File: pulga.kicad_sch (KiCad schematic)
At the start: 32 parts, among them J1 Conn_01x04_Pin, J2 Conn_01x04_Pin, SW1 SW_Push, SW2 SW_Push, U2 ESP32-C3-WROOM-02, U3 TCAN332G, U4 AMS1117-3.3

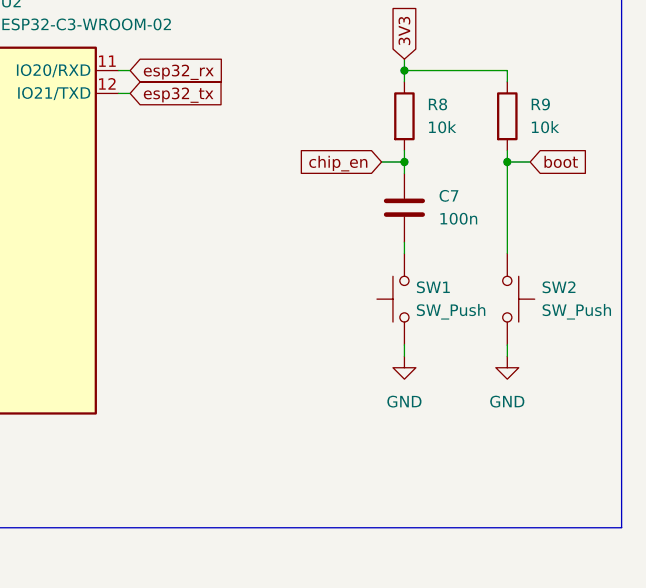
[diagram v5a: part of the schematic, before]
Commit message: corrigindo a posição de C7 para ficar em paralelo em relação a SW1
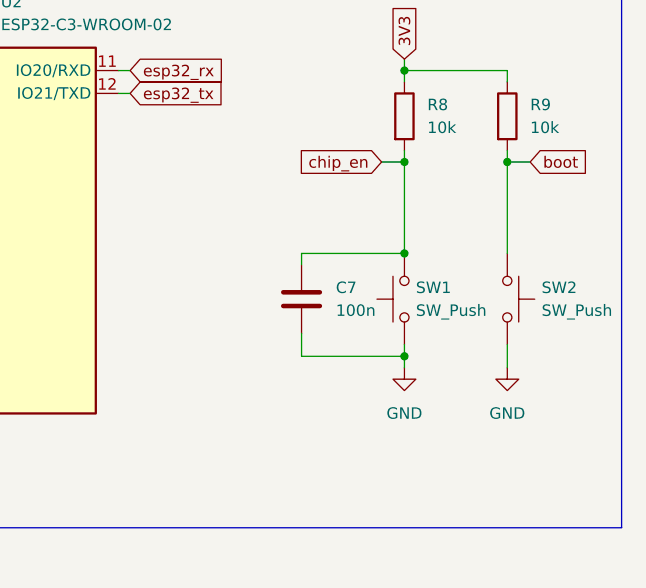
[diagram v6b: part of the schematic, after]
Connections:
- net GND: now also C7.2
- net chip_en: now also SW1.2
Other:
- moved on the sheet: C7
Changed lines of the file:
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@@
 	)
 	(junction
-		(at 256.54 55.88)
-		(diameter 0)
-		(color 0 0 0 0)
-	)
-	(junction
 		(at 46.99 55.88)
 		(diameter 0)
@@
 	)
 	(junction
+		(at 256.54 66.04)
+		(diameter 0)
+		(color 0 0 0 0)
+	)
+	(junction
 		(at 38.1 55.88)
 		(diameter 0)
@@
 	)
 	(junction
+		(at 256.54 77.47)
+		(diameter 0)
+		(color 0 0 0 0)
+	)
+	(junction
 		(at 38.1 33.02)
 		(diameter 0)
@@
 		(color 0 0 0 0)
 	)
+	(junction
+		(at 256.54 55.88)
+		(diameter 0)
+		(color 0 0 0 0)
+	)
 	(wire
 		(pts
@@
 	(wire
 		(pts
-			(xy 267.97 76.2) (xy 267.97 77.47)
+			(xy 256.54 54.61) (xy 256.54 55.88)
+		)
+		(stroke
+			(width 0)
+			(type default)
+		)
+	)
+	(wire
+		(pts
+			(xy 267.97 76.2) (xy 267.97 78.74)
 		)
 		(stroke
@@
 	(wire
 		(pts
+			(xy 245.11 74.93) (xy 245.11 77.47)
+		)
+		(stroke
+			(width 0)
+			(type default)
+		)
+	)
+	(wire
+		(pts
 			(xy 113.03 146.05) (xy 113.03 143.51)
 		)
@@
 	(wire
 		(pts
+			(xy 256.54 55.88) (xy 256.54 66.04)
+		)
+		(stroke
+			(width 0)
+			(type default)
+		)
+	)
+	(wire
+		(pts
 			(xy 237.49 120.65) (xy 240.03 120.65)
 		)
@@
 	(wire
 		(pts
+			(xy 245.11 77.47) (xy 256.54 77.47)
+		)
+		(stroke
+			(width 0)
+			(type default)
+		)
+	)
+	(wire
+		(pts
 			(xy 209.55 86.36) (xy 209.55 87.63)
 		)
@@
 	(wire
 		(pts
-			(xy 256.54 64.77) (xy 256.54 66.04)
-		)
-		(stroke
-			(width 0)
-			(type default)
-		)
-	)
-	(wire
-		(pts
 			(xy 54.61 146.05) (xy 55.88 146.05)
 		)
@@
 	(wire
 		(pts
+			(xy 245.11 66.04) (xy 256.54 66.04)
+		)
+		(stroke
+			(width 0)
+			(type default)
+		)
+	)
+	(wire
+		(pts
 			(xy 44.45 146.05) (xy 46.99 146.05)
 		)
@@
 	(wire
 		(pts
-			(xy 256.54 55.88) (xy 256.54 57.15)
-		)
-		(stroke
-			(width 0)
-			(type default)
-		)
-	)
-	(wire
-		(pts
 			(xy 256.54 76.2) (xy 256.54 77.47)
 		)
@@
 	(wire
 		(pts
-			(xy 256.54 54.61) (xy 256.54 55.88)
+			(xy 36.83 30.48) (xy 38.1 30.48)
 		)
 		(stroke
@@
 	(wire
 		(pts
-			(xy 36.83 30.48) (xy 38.1 30.48)
+			(xy 256.54 78.74) (xy 256.54 77.47)
 		)
 		(stroke
@@
 	(wire
 		(pts
+			(xy 245.11 67.31) (xy 245.11 66.04)
+		)
+		(stroke
+			(width 0)
+			(type default)
+		)
+	)
+	(wire
+		(pts
 			(xy 78.74 161.29) (xy 78.74 162.56)
 		)
@@
 	(symbol
 		(lib_id "Device:C")
-		(at 256.54 60.96 0)
+		(at 245.11 71.12 0)
 		(unit 1)
 		(exclude_from_sim no)
@@
 		(fields_autoplaced yes)
 		(property "Reference" "C7"
-			(at 260.35 59.6899 0)
+			(at 248.92 69.8499 0)
 			(effects
 				(font
@@
 		)
 		(property "Value" "100n"
-			(at 260.35 62.2299 0)
+			(at 248.92 72.3899 0)
 			(effects
 				(font
@@
 		)
 		(property "Footprint" "Capacitor_SMD:C_0201_0603Metric"
-			(at 257.5052 64.77 0)
+			(at 246.0752 74.93 0)
 			(effects
 				(font
@@
 		)
 		(property "Datasheet" "~"
-			(at 256.54 60.96 0)
+			(at 245.11 71.12 0)
 			(effects
 				(font
@@
 		)
 		(property "Description" "Unpolarized capacitor"
-			(at 256.54 60.96 0)
+			(at 245.11 71.12 0)
 			(effects
 				(font
@@
 	(symbol
 		(lib_id "power:GND")
-		(at 256.54 77.47 0)
+		(at 256.54 78.74 0)
 		(unit 1)
 		(exclude_from_sim no)
@@
 		(fields_autoplaced yes)
 		(property "Reference" "#PWR07"
-			(at 256.54 83.82 0)
+			(at 256.54 85.09 0)
 			(effects
 				(font
@@
 		)
 		(property "Value" "GND"
-			(at 256.54 82.55 0)
+			(at 256.54 83.82 0)
 			(effects
 				(font
@@
 		)
 		(property "Footprint" ""
-			(at 256.54 77.47 0)
+			(at 256.54 78.74 0)
 			(effects
 				(font
@@
 		)
 		(property "Datasheet" ""
-			(at 256.54 77.47 0)
+			(at 256.54 78.74 0)
 			(effects
 				(font
@@
 		)
 		(property "Description" "Power symbol creates a global label with name \"GND\" , ground"
-			(at 256.54 77.47 0)
+			(at 256.54 78.74 0)
 			(effects
 				(font
@@
 	(symbol
 		(lib_id "power:GND")
-		(at 267.97 77.47 0)
+		(at 267.97 78.74 0)
 		(unit 1)
 		(exclude_from_sim no)
@@
 		(fields_autoplaced yes)
 		(property "Reference" "#PWR08"
-			(at 267.97 83.82 0)
+			(at 267.97 85.09 0)
 			(effects
 				(font
@@
 		)
 		(property "Value" "GND"
-			(at 267.97 82.55 0)
+			(at 267.97 83.82 0)
 			(effects
 				(font
@@
 		)
 		(property "Footprint" ""
-			(at 267.97 77.47 0)
+			(at 267.97 78.74 0)
 			(effects
 				(font
@@
 		)
 		(property "Datasheet" ""
-			(at 267.97 77.47 0)
+			(at 267.97 78.74 0)
 			(effects
 				(font
@@
 		)
 		(property "Description" "Power symbol creates a global label with name \"GND\" , ground"
-			(at 267.97 77.47 0)
+			(at 267.97 78.74 0)
 			(effects
 				(font

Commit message: adicionando o LCSC dos botões de bootstrap do esp32
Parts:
- SW1, SW2: LCSC (none) -> C231329
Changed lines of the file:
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@@
+			)
+		)
+		(property "LCSC" "C231329"
+			(at 256.54 71.12 90)
+			(effects
+				(font
+					(size 1.27 1.27)
+				)
+				(hide yes)
 			)
 		)
@@
 			(effects
 				(font
+					(size 1.27 1.27)
+				)
+				(hide yes)
+			)
+		)
+		(property "LCSC" "C231329"
+			(at 267.97 71.12 90)
+			(effects
+				(font

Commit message: adicionei o LCSC no TCAN332x
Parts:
- U3: LCSC (none) -> C544741
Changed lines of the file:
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@@
+			)
+		)
+		(property "LCSC" "C544741"
+			(at 78.74 151.13 0)
+			(effects
+				(font
+					(size 1.27 1.27)
+				)
+				(hide yes)
 			)
 		)
